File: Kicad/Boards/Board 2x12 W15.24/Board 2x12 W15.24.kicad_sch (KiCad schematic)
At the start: 3 parts, among them J1 Conn_02x12_Counter_Clockwise, J2 Pin_Header_01x12, J3 Pin_Header_01x12

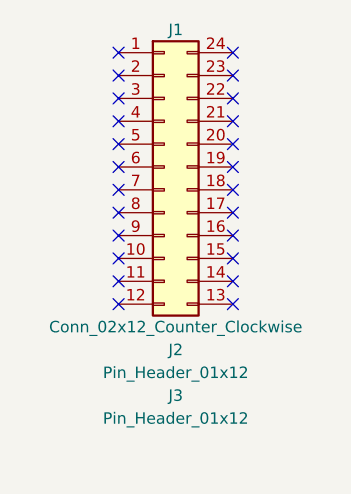
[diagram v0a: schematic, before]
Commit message: Updated the empty board schematics 2x06 and 2x12 for nicer board symbols.
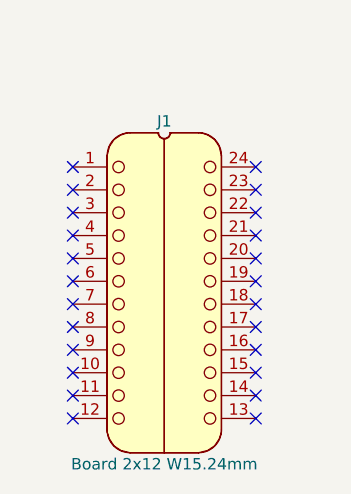
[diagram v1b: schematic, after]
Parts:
- removed J2, J3: Pin_Header_01x12, SamacSys_Parts:PinHeader_1x12_P2.54mm_Vertical, symbol HCP65:Pin_Header_01x16
- J1: value Conn_02x12_Counter_Clockwise -> Board 2x12 W15.24mm; footprint (none) -> SamacSys_Parts:DIP-24_Board_W15.24mm; symbol Connector_Generic:Conn_02x12_Counter_Clockwise -> HCP65:Board_02x12_W15.24mm
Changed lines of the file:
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@@
 	)
 	(no_connect
-		(at 45.72 72.39)
+		(at 48.26 85.09)
 	)
 	(no_connect
-		(at 33.02 82.55)
+		(at 27.94 95.25)
 	)
 	(no_connect
-		(at 45.72 57.15)
+		(at 48.26 69.85)
 	)
 	(no_connect
-		(at 33.02 64.77)
+		(at 27.94 77.47)
 	)
 	(no_connect
-		(at 33.02 72.39)
+		(at 27.94 85.09)
 	)
 	(no_connect
-		(at 33.02 74.93)
+		(at 27.94 87.63)
 	)
 	(no_connect
-		(at 33.02 62.23)
+		(at 27.94 74.93)
 	)
 	(no_connect
-		(at 45.72 74.93)
+		(at 48.26 87.63)
 	)
 	(no_connect
-		(at 33.02 80.01)
+		(at 27.94 92.71)
 	)
 	(no_connect
-		(at 33.02 67.31)
+		(at 27.94 80.01)
 	)
 	(no_connect
-		(at 45.72 69.85)
+		(at 48.26 82.55)
 	)
 	(no_connect
-		(at 45.72 62.23)
+		(at 48.26 74.93)
 	)
 	(no_connect
-		(at 33.02 57.15)
+		(at 27.94 69.85)
 	)
 	(no_connect
-		(at 45.72 80.01)
+		(at 48.26 92.71)
 	)
 	(no_connect
-		(at 33.02 77.47)
+		(at 27.94 90.17)
 	)
 	(no_connect
-		(at 45.72 82.55)
+		(at 48.26 95.25)
 	)
 	(no_connect
-		(at 33.02 85.09)
+		(at 27.94 97.79)
 	)
 	(no_connect
-		(at 33.02 69.85)
+		(at 27.94 82.55)
 	)
 	(no_connect
-		(at 45.72 67.31)
+		(at 48.26 80.01)
 	)
 	(no_connect
-		(at 45.72 85.09)
+		(at 48.26 97.79)
 	)
 	(no_connect
-		(at 33.02 59.69)
+		(at 27.94 72.39)
 	)
 	(no_connect
-		(at 45.72 77.47)
+		(at 48.26 90.17)
 	)
 	(no_connect
-		(at 45.72 64.77)
+		(at 48.26 77.47)
 	)
 	(no_connect
-		(at 45.72 59.69)
+		(at 48.26 72.39)
 	)
 	(symbol
-		(lib_id "HCP65:Pin_Header_01x16")
-		(at 39.37 91.44 0)
-		(mirror y)
+		(lib_id "HCP65:Board_02x12_W15.24mm")
+		(at 38.1 69.85 0)
 		(unit 1)
 		(exclude_from_sim no)
@@
 		(on_board yes)
 		(dnp no)
-		(property "Reference" "J2"
-			(at 39.37 90.17 0)
+		(property "Reference" "J1"
+			(at 38.1 64.77 0)
 			(effects
 				(font
@@
 			)
 		)
-		(property "Value" "Pin_Header_01x12"
-			(at 39.37 92.71 0)
+		(property "Value" "Board 2x12 W15.24mm"
+			(at 38.1 102.87 0)
 			(effects
 				(font
@@
 			)
 		)
-		(property "Footprint" "SamacSys_Parts:PinHeader_1x12_P2.54mm_Vertical"
-			(at 39.37 95.25 0)
+		(property "Footprint" "SamacSys_Parts:DIP-24_Board_W15.24mm"
+			(at 38.1 105.41 0)
 			(effects
 				(font
@@
 			)
 		)
-		(property "Datasheet" "~"
-			(at 44.45 91.44 0)
+		(property "Datasheet" ""
+			(at 38.1 115.57 0)
 			(effects
 				(font
@@
 		)
 		(property "Description" ""
-			(at 39.37 91.44 0)
-			(effects
-				(font
-					(size 1.27 1.27)
-				)
-				(hide yes)
-			)
-		)
-		(instances
-			(project "Device Decode stage A"
-				(path "/337b5f72-8be1-4121-9dc6-479b565482b2"
-					(reference "J2")
-					(unit 1)
-				)
-			)
-		)
-	)
-	(symbol
-		(lib_id "Connector_Generic:Conn_02x12_Counter_Clockwise")
-		(at 38.1 69.85 0)
-		(unit 1)
-		(exclude_from_sim no)
-		(in_bom yes)
-		(on_board yes)
-		(dnp no)
-		(property "Reference" "J1"
-			(at 39.37 54.61 0)
-			(effects
-				(font
-					(size 1.27 1.27)
-				)
-			)
-		)
-		(property "Value" "Conn_02x12_Counter_Clockwise"
-			(at 39.37 87.63 0)
-			(effects
-				(font
-					(size 1.27 1.27)
-				)
-			)
-		)
-		(property "Footprint" ""
-			(at 38.1 69.85 0)
-			(effects
-				(font
-					(size 1.27 1.27)
-				)
-				(hide yes)
-			)
-		)
-		(property "Datasheet" "~"
-			(at 38.1 69.85 0)
-			(effects
-				(font
-					(size 1.27 1.27)
-				)
-				(hide yes)
-			)
-		)
-		(property "Description" "Generic connector, double row, 02x12, counter clockwise pin numbering scheme (similar to DIP package numbering), script generated (kicad-library-utils/schlib/autogen/connector/)"
-			(at 38.1 69.85 0)
+			(at 38.1 87.63 0)
 			(effects
 				(font
@@
 					(unit 1)
 				)
-			)
-		)
-	)
-	(symbol
-		(lib_id "HCP65:Pin_Header_01x16")
-		(at 39.37 96.52 0)
-		(unit 1)
-		(exclude_from_sim no)
-		(in_bom yes)
-		(on_board yes)
-		(dnp no)
-		(property "Reference" "J3"
-			(at 39.37 95.25 0)
-			(effects
-				(font
-					(size 1.27 1.27)
-				)
-			)
-		)
-		(property "Value" "Pin_Header_01x12"
-			(at 39.37 97.79 0)
-			(effects
-				(font
-					(size 1.27 1.27)
-				)
-			)
-		)
-		(property "Footprint" "SamacSys_Parts:PinHeader_1x12_P2.54mm_Vertical"
-			(at 39.37 100.33 0)
-			(effects
-				(font
-					(size 1.27 1.27)
-				)
-				(hide yes)
-			)
-		)
-		(property "Datasheet" "~"
-			(at 34.29 96.52 0)
-			(effects
-				(font
-					(size 1.27 1.27)
-				)
-				(hide yes)
-			)
-		)
-		(property "Description" ""
-			(at 39.37 96.52 0)
-			(effects
-				(font
-					(size 1.27 1.27)
-				)
-				(hide yes)
-			)
-		)
-		(instances
-			(project "Device Decode stage A"
-				(path "/337b5f72-8be1-4121-9dc6-479b565482b2"
-					(reference "J3")
-					(unit 1)
-				)
